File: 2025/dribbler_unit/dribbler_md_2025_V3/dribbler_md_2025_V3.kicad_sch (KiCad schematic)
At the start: 103 parts, among them J2 Conn_01x04_Pin, J3 Conn_01x02_Pin, J4 Conn_01x07_Pin, J5 Conn_01x03_Pin, J6 Conn_01x02_Pin, J7 Conn_01x02_Pin, J8 Conn_01x02_Socket, SW2 SW_MEC_5E, SW4 SW_MEC_5E, U1 MAX3051, U2 STS8DN3LLH5, U3 STS8DN3LLH5, U4 DRV8701, U5 STM32F446RETx, Y1 Crystal_GND2

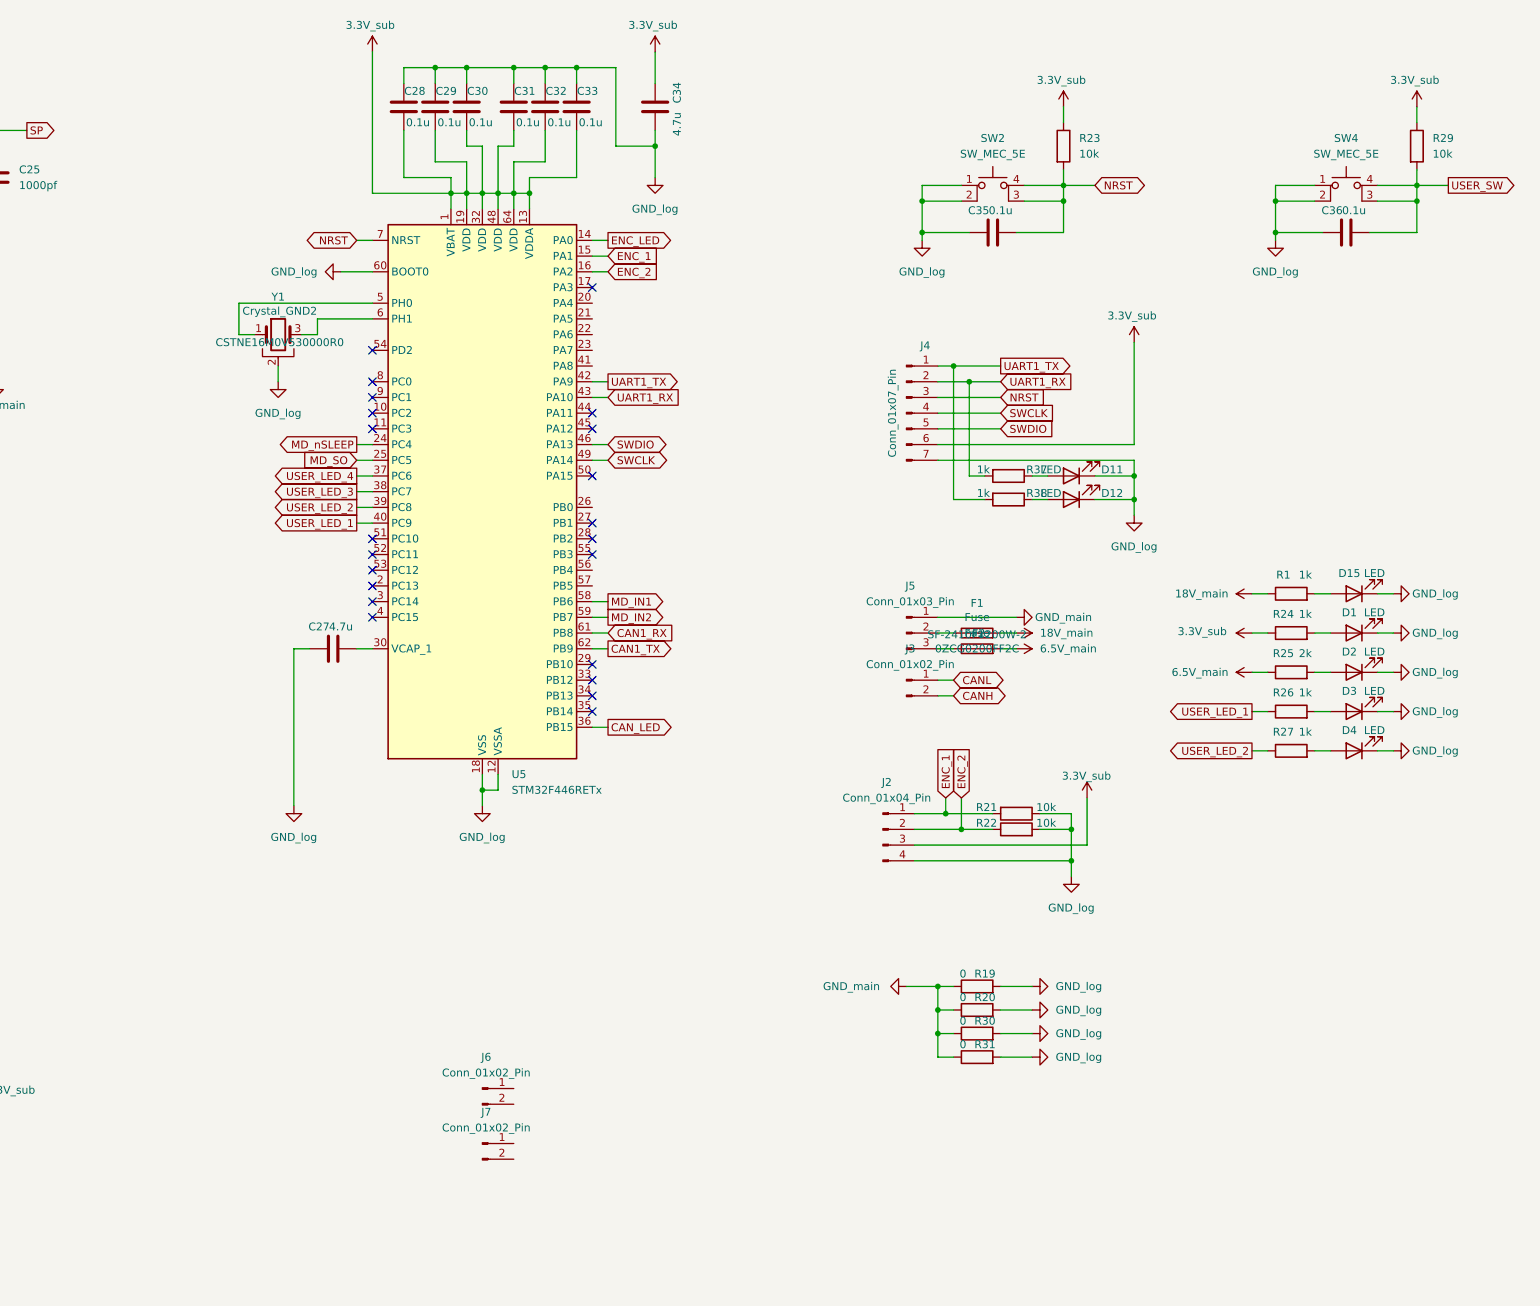
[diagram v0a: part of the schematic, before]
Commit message: ボールセンサの回路追加＆446のピン配置変更
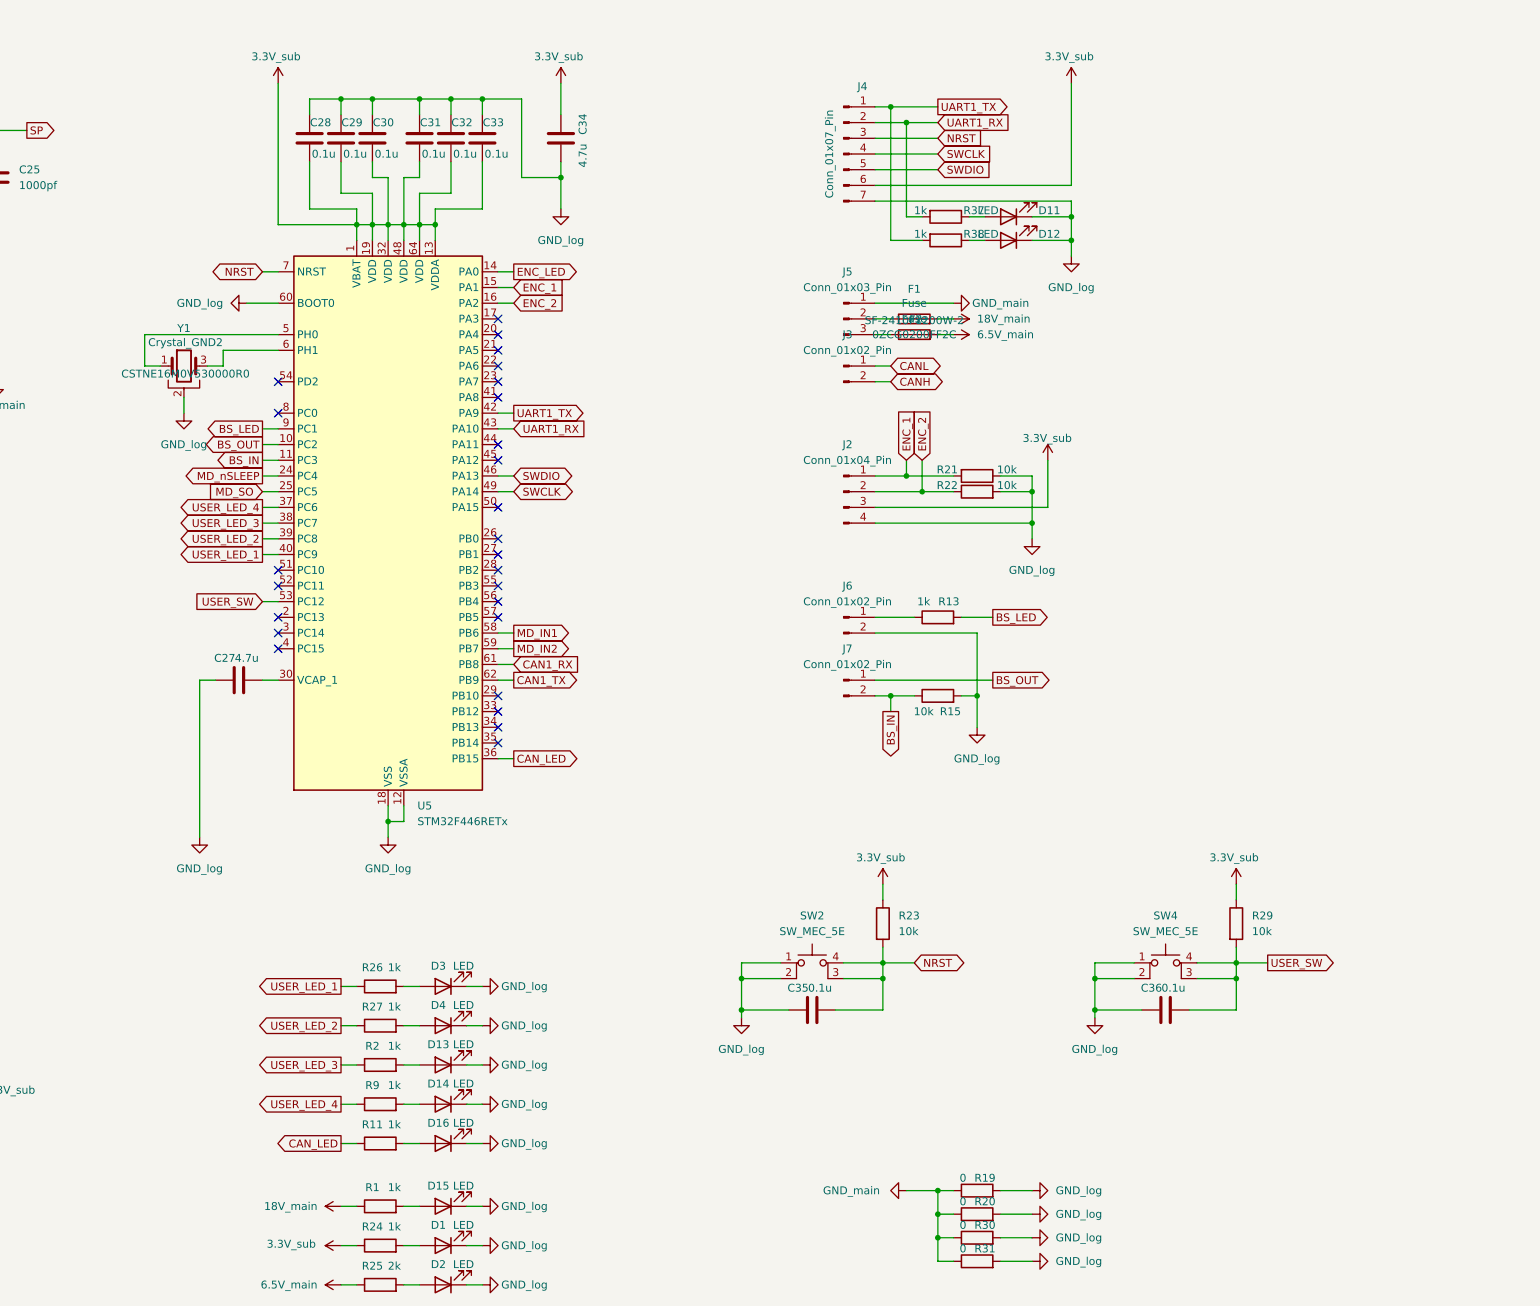
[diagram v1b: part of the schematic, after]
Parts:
- added D13, D14, D16: LED, dribbler_md:LED_1608_user_dif, symbol Device:LED
- added R11, R13, R2, R9: 1k, Resistor_SMD:R_0603_1608Metric_Pad0.98x0.95mm_HandSolder, symbol Device:R
- added R15: 10k, Resistor_SMD:R_0603_1608Metric_Pad0.98x0.95mm_HandSolder, symbol Device:R
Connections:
- net CAN_LED: now also R11.1
- net GND_log: now also J6.2 (Pin_2), D13.1 (K), D14.1 (K), D16.1 (K), R15.2
- net USER_LED_3: now also R2.1
- net USER_LED_4: now also R9.1
- net USER_SW: now also U5.53 (PC12)
- net BS_OUT: now reaches U5.10 (PC2)
- net BS_OUT: now also J7.1 (Pin_1)
- net BS_IN: now reaches U5.11 (PC3)
- net BS_IN: now also J7.2 (Pin_2), R15.1
- net BS_LED: now reaches U5.9 (PC1)
- net BS_LED: now also R13.2
- net at J6.1 (Pin_1): now also R13.1
- new net: D13.2 (A), R2.2
- new net: D14.2 (A), R9.2
- new net: D16.2 (A), R11.2
- no-connect marks 22 -> 26
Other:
- moved on the sheet: C27, C28, C29, C30, C31, C32, C33, C34, C35, C36, D1, D11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

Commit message: MD再配線
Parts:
- added R39: 0, Resistor_SMD:R_0603_1608Metric_Pad0.98x0.95mm_HandSolder, symbol Device:R
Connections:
- net GND_log: now also R39.2
- net GND_main: now also R39.1
- net MD_IN1: now also U5.22 (PA6); no longer U5.58 (PB6)
- net MD_IN2: now also U5.23 (PA7); no longer U5.59 (PB7)
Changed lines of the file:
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@@
 	(paper "A3")
 	(junction
+		(at 312.42 219.71)
+		(diameter 0)
+		(color 0 0 0 0)
+	)
+	(junction
 		(at 87.63 54.61)
 		(diameter 0)
@@
 	)
 	(no_connect
-		(at 241.3 74.93)
-	)
-	(no_connect
 		(at 241.3 128.27)
 	)
@@
 	)
 	(no_connect
-		(at 241.3 77.47)
+		(at 241.3 135.89)
 	)
 	(no_connect
-		(at 241.3 135.89)
+		(at 241.3 118.11)
 	)
 	(no_connect
@@
 	)
 	(no_connect
+		(at 241.3 120.65)
+	)
+	(no_connect
 		(at 241.3 115.57)
 	)
@@
 	(wire
 		(pts
-			(xy 241.3 120.65) (xy 243.84 120.65)
+			(xy 241.3 77.47) (xy 243.84 77.47)
 		)
 		(stroke
@@
 	(wire
 		(pts
+			(xy 322.58 223.52) (xy 327.66 223.52)
+		)
+		(stroke
+			(width 0)
+			(type default)
+		)
+	)
+	(wire
+		(pts
 			(xy 128.27 64.77) (xy 128.27 62.23)
 		)
@@
 	(wire
 		(pts
+			(xy 312.42 223.52) (xy 314.96 223.52)
+		)
+		(stroke
+			(width 0)
+			(type default)
+		)
+	)
+	(wire
+		(pts
 			(xy 251.46 44.45) (xy 251.46 49.53)
 		)
@@
 	(wire
 		(pts
+			(xy 312.42 219.71) (xy 312.42 223.52)
+		)
+		(stroke
+			(width 0)
+			(type default)
+		)
+	)
+	(wire
+		(pts
 			(xy 203.2 125.73) (xy 205.74 125.73)
 		)
@@
 	(wire
 		(pts
-			(xy 241.3 118.11) (xy 243.84 118.11)
+			(xy 241.3 74.93) (xy 243.84 74.93)
 		)
 		(stroke
@@
 	(global_label "MD_IN2"
 		(shape output)
-		(at 243.84 120.65 0)
+		(at 243.84 77.47 0)
 		(fields_autoplaced yes)
 		(effects
@@
 		)
 		(property "Intersheetrefs" "${INTERSHEET_REFS}"
-			(at 253.659 120.65 0)
+			(at 253.659 77.47 0)
 			(effects
 				(font
@@
 	(global_label "MD_IN1"
 		(shape output)
-		(at 243.84 118.11 0)
+		(at 243.84 74.93 0)
 		(fields_autoplaced yes)
 		(effects
@@
 		)
 		(property "Intersheetrefs" "${INTERSHEET_REFS}"
-			(at 253.659 118.11 0)
+			(at 253.659 74.93 0)
 			(effects
 				(font
@@
 	)
 	(symbol
+		(lib_id "power:GND")
+		(at 327.66 223.52 90)
+		(unit 1)
+		(exclude_from_sim no)
+		(in_bom yes)
+		(on_board yes)
+		(dnp no)
+		(fields_autoplaced yes)
+		(property "Reference" "#PWR054"
+			(at 334.01 223.52 0)
+			(effects
+				(font
+					(size 1.27 1.27)
+				)
+				(hide yes)
+			)
+		)
+		(property "Value" "GND_log"
+			(at 331.47 223.5199 90)
+			(effects
+				(font
+					(size 1.27 1.27)
+				)
+				(justify right)
+			)
+		)
+		(property "Footprint" ""
+			(at 327.66 223.52 0)
+			(effects
+				(font
+					(size 1.27 1.27)
+				)
+				(hide yes)
+			)
+		)
+		(property "Datasheet" ""
+			(at 327.66 223.52 0)
+			(effects
+				(font
+					(size 1.27 1.27)
+				)
+				(hide yes)
+			)
+		)
+		(property "Description" "Power symbol creates a global label with name \"GND\" , ground"
+			(at 327.66 223.52 0)
+			(effects
+				(font
+					(size 1.27 1.27)
+				)
+				(hide yes)
+			)
+		)
+		(pin "1"
+		)
+		(instances
+			(project "dribbler_md_2025_V3"
+				(path "/fb031fd6-d0d1-41bb-b086-03f1e4d4d794"
+					(reference "#PWR054")
+					(unit 1)
+				)
+			)
+		)
+	)
+	(symbol
 		(lib_id "power:VDD")
 		(at 72.39 91.44 0)
@@
 					(unit 1)
 				)
+			)
+		)
+	)
+	(symbol
+		(lib_id "Device:R")
+		(at 318.77 223.52 90)
+		(unit 1)
+		(exclude_from_sim no)
+		(in_bom yes)
+		(on_board yes)
+		(dnp no)
+		(property "Reference" "R39"
+			(at 320.04 221.488 90)
+			(effects
+				(font
+					(size 1.27 1.27)
+				)
+			)
+		)
+		(property "Value" "0"
+			(at 316.484 221.488 90)
+			(effects
+				(font
+					(size 1.27 1.27)
+				)
+			)
+		)
+		(property "Footprint" "Resistor_SMD:R_0603_1608Metric_Pad0.98x0.95mm_HandSolder"
+			(at 318.77 225.298 90)
+			(effects
+				(font
+					(size 1.27 1.27)
+				)
+				(hide yes)
+			)
+		)
+		(property "Datasheet" "~"
+			(at 318.77 223.52 0)
+			(effects
+				(font
+					(size 1.27 1.27)
+				)
+				(hide yes)
+			)
+		)
+		(property "Description" "Resistor"
+			(at 318.77 223.52 0)
+			(effects
+				(font
+					(size 1.27 1.27)
+				)
+				(hide yes)
+			)
+		)
+		(pin "1"
+		)
+		(pin "2"
+		)
+		(instances
+			(project "dribbler_md_2025_V3"
+				(path "/fb031fd6-d0d1-41bb-b086-03f1e4d4d794"
+					(reference "R39")
+					(unit 1)
+				)

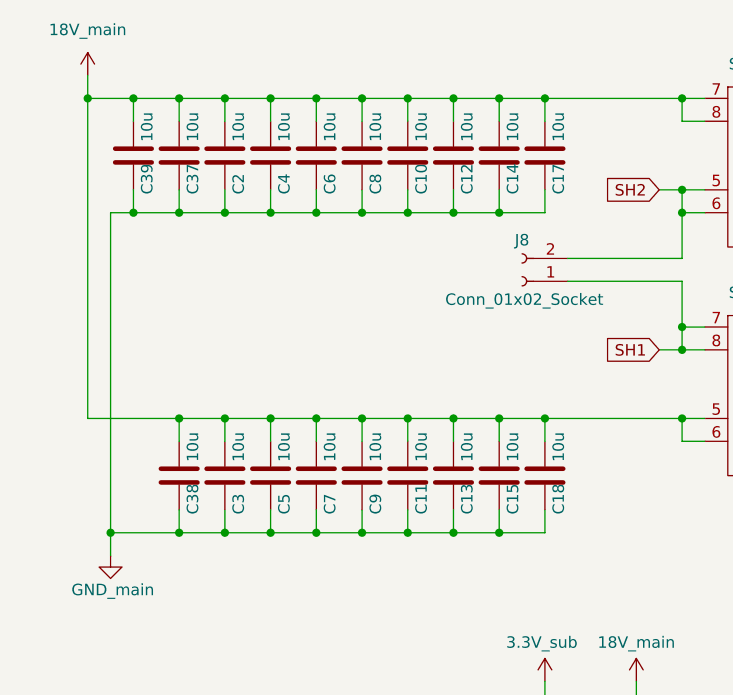
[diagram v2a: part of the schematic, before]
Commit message: ダイオード挿入
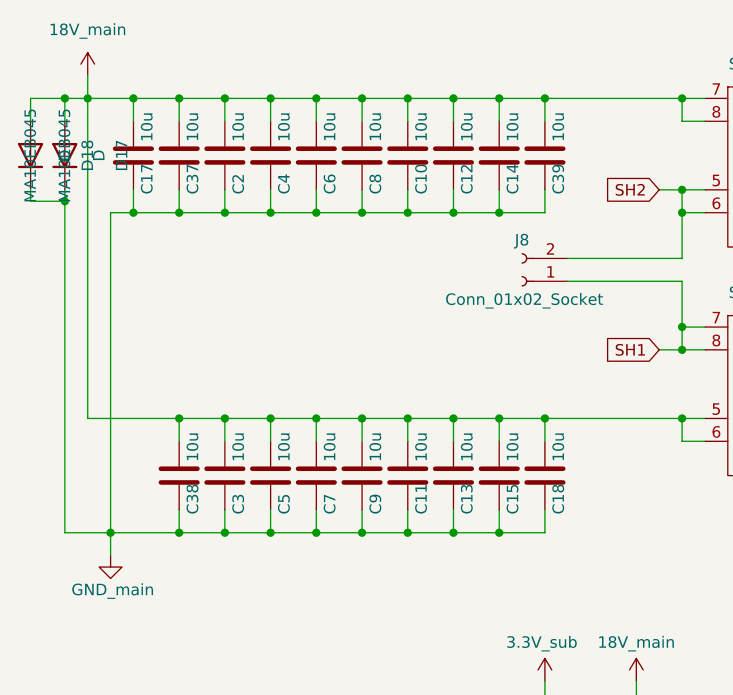
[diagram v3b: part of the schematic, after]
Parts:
- added D17, D18: D, dribbler_md:MA10EB045, symbol Device:D
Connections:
- net 18V_main: now also D17.2 (A), D18.2 (A)
- net GND_main: now also D17.1 (K), D18.1 (K)
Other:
- moved on the sheet: C39

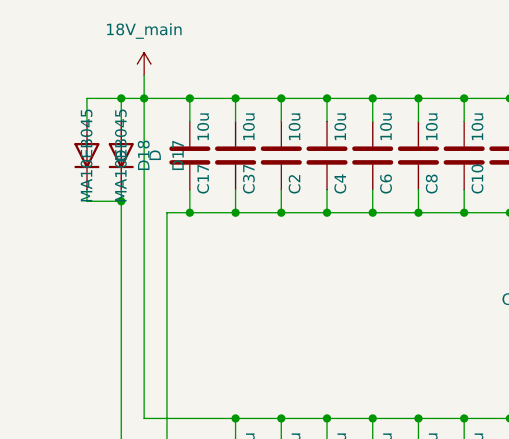
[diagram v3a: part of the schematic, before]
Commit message: 電源周りの配線完了
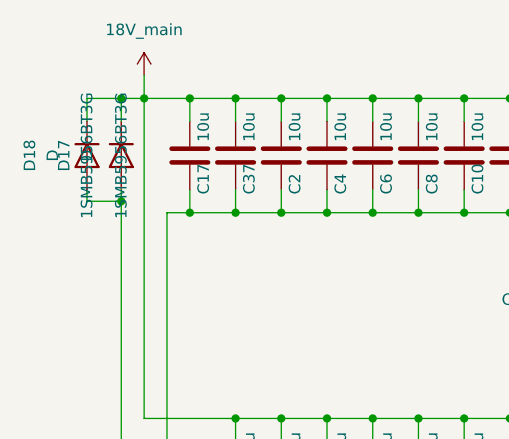
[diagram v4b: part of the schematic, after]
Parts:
- D17, D18: footprint dribbler_md:MA10EB045 -> dribbler_md:1SMB5956BT3G
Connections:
- net 18V_main: now also D17.1 (K), D18.1 (K); no longer D17.2 (A), D18.2 (A)
- net GND_main: now also D17.2 (A), D18.2 (A); no longer D17.1 (K), D18.1 (K)
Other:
- moved on the sheet: D17, D18
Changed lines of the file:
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@@
 	(symbol
 		(lib_id "Device:D")
-		(at 19.05 33.02 90)
+		(at 19.05 33.02 270)
 		(unit 1)
 		(exclude_from_sim no)
@@
 		(dnp no)
 		(property "Reference" "D17"
-			(at 25.4 33.02 0)
+			(at 12.7 33.02 0)
 			(effects
 				(font
@@
 		)
 		(property "Value" "D"
-			(at 22.86 33.02 0)
+			(at 15.24 33.02 0)
 			(effects
 				(font
@@
 			)
 		)
-		(property "Footprint" "dribbler_md:MA10EB045"
+		(property "Footprint" "dribbler_md:1SMB5956BT3G"
 			(at 19.05 33.02 0)
 			(effects
@@
 			)
 		)
-		(property "Description" "MA10EB045"
+		(property "Description" "1SMB5956BT3G"
 			(at 19.05 33.02 0)
 			(effects
@@
 	(symbol
 		(lib_id "Device:D")
-		(at 15.24 33.02 90)
+		(at 15.24 33.02 270)
 		(unit 1)
 		(exclude_from_sim no)
@@
 		(dnp no)
 		(property "Reference" "D18"
-			(at 21.59 33.02 0)
+			(at 8.89 33.02 0)
 			(effects
 				(font
@@
 		)
 		(property "Value" "D"
-			(at 19.05 33.02 0)
+			(at 11.43 33.02 0)
 			(effects
 				(font
@@
 			)
 		)
-		(property "Footprint" "dribbler_md:MA10EB045"
+		(property "Footprint" "dribbler_md:1SMB5956BT3G"
 			(at 15.24 33.02 0)
 			(effects
@@
 			)
 		)
-		(property "Description" "MA10EB045"
+		(property "Description" "1SMB5956BT3G"
 			(at 15.24 33.02 0)
 			(effects
